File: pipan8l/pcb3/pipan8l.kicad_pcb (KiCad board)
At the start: 2 copper layers, 262.3 x 76.2 mm, 64 parts, among them J1 2x18edgecon, J2 2x18edgecon, J3 2x18edgecon, J4 2x18edgecon, J5 Conn_02x20_Odd_Even, J6 Conn_01x02_Pin, J7 Conn_01x16, J8 Conn_01x12, Q1 2N3906, Q10 2N3906, Q11 2N3906, Q12 2N3906, Q13 2N3906, Q14 2N3906, Q15 2N3906, Q16 2N3906, Q17 2N7000, Q18 2N7000, Q2 2N3906, Q3 2N3906, Q4 2N3906, Q5 2N3906, Q6 2N3906, Q7 2N3906, Q8 2N3906, Q9 2N3906, U1 MCP23017, U2 MCP23017, U3 MCP23017, U4 MCP23017

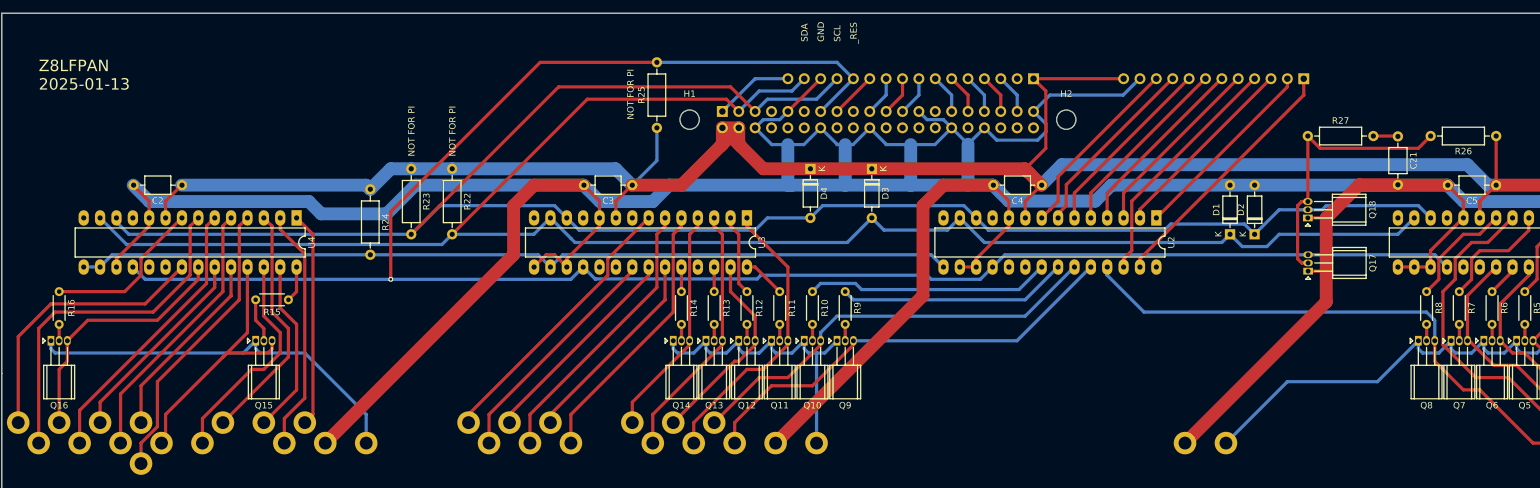
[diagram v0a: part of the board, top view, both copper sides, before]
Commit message: revert pipan8l/pcb3 front-panel piggy-back board to 2025-01-02
it is good enough as is and don't want to make new boards
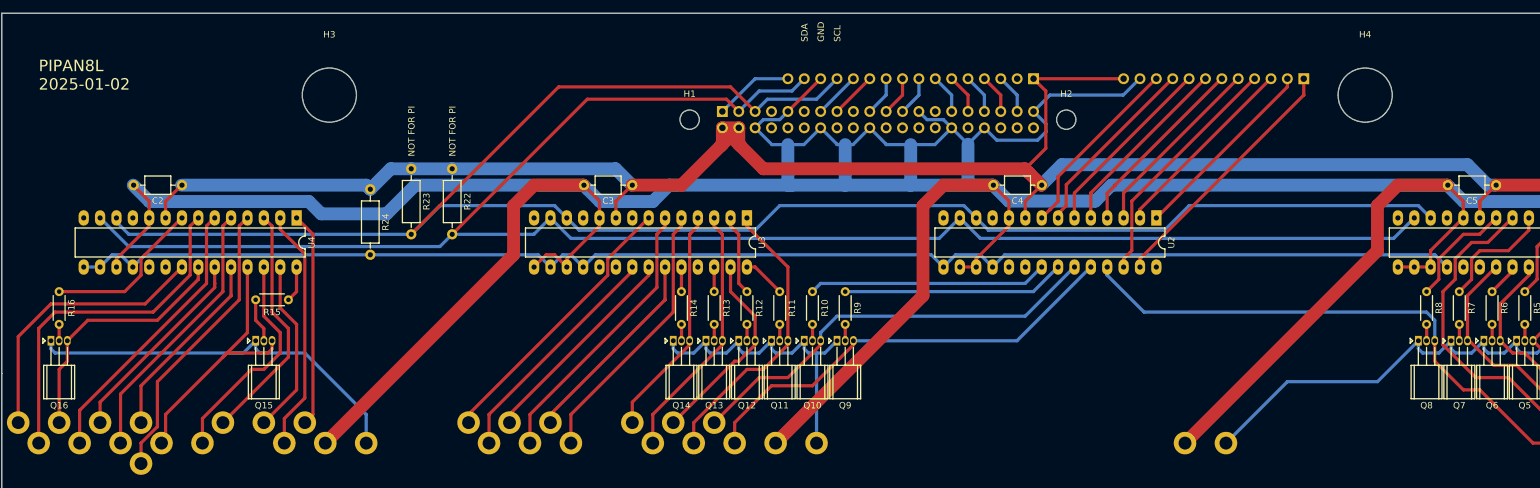
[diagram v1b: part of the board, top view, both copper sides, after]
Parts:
- removed C21: 0.01u, Capacitor_THT:C_Axial_L3.8mm_D2.6mm_P7.50mm_Horizontal
- removed D1, D2, D3, D4: 1N4148, Diode_THT:D_DO-35_SOD27_P7.62mm_Horizontal
- removed Q17, Q18: 2N7000, Package_TO_SOT_THT:TO-92_Inline_W4.0mm_Horizontal_FlatSideDown
- removed R25: 2.2K, Resistor_THT:R_Axial_DIN0207_L6.3mm_D2.5mm_P10.16mm_Horizontal
- removed R26: 100K, Resistor_THT:R_Axial_DIN0207_L6.3mm_D2.5mm_P10.16mm_Horizontal
- removed R27: 100, Resistor_THT:R_Axial_DIN0207_L6.3mm_D2.5mm_P10.16mm_Horizontal
- added H3: MountingHole, MountingHole:MountingHole_8.4mm_M8, F.Cu at (50.8, 12.7)
- added H4: MountingHole, MountingHole:MountingHole_8.4mm_M8, F.Cu at (211.5, 12.7)
- J1: footprint myz8lfpanfoots:backpins-A -> mypipan8lfoots:backpins-A
- J2: footprint myz8lfpanfoots:backpins-B -> mypipan8lfoots:backpins-B
- J3: footprint myz8lfpanfoots:backpins-C -> mypipan8lfoots:backpins-C
- J4: footprint myz8lfpanfoots:backpins-D -> mypipan8lfoots:backpins-D
- R22: value 1.2K -> 1K
- R23: value 680 -> 1K
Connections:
- J5 pad 13: /_RESET -> /GPIO27
- J7 pad 12: /_RESET -> /GPIO27
- U1 pad 18: /_RESET -> /PULLUP
- U2 pad 18: /_RESET -> /PULLUP
- U3 pad 18: /_RESET -> /PULLUP
- U4 pad 18: /_RESET -> /PULLUP
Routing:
- net /_RESET: track 375.2 -> 0.00 mm, vias 1 -> 0
- net /PULLUP: track 136.5 -> 220.8 mm
- net Net-(Q17-G): track 42.8 -> 0.00 mm
- net VCC: track 326.5 -> 308.5 mm
- net GND: track 681.7 -> 672.2 mm
- net /GPIO27: track 0.00 -> 7.18 mm
- net /SDA: track 282.9 -> 279.0 mm
- net Net-(C21-Pad1): track 3.75 -> 0.00 mm
- net /SCL: track 294.1 -> 292.8 mm
- net /RSR09: track 35.6 -> 34.6 mm
- net /RSR10: track 37.9 -> 37.1 mm
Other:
- board text added: "PIPAN8L 2025-01-02"
- board text removed: "Z8LFPAN 2025-01-13"
- board text removed: "_RES"

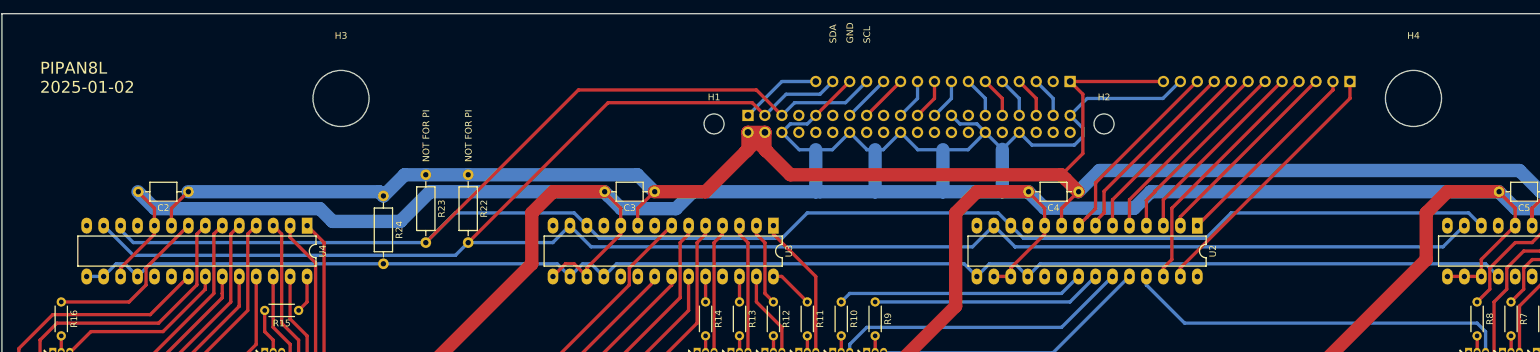
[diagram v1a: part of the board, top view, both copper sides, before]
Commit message: add clipping diodes to i2c bus for zynq-connected front panel
also add _RESET line as 4th pin on connector
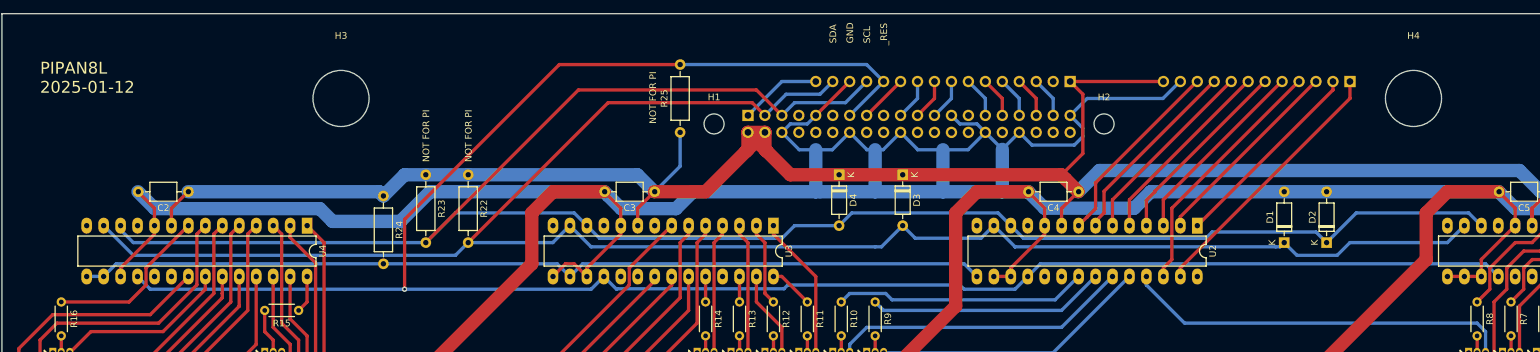
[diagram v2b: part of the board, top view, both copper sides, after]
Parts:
- added D1: 1N4148, Diode_THT:D_DO-35_SOD27_P7.62mm_Horizontal, F.Cu at (192.1, 34.3)
- added D2: 1N4148, Diode_THT:D_DO-35_SOD27_P7.62mm_Horizontal, F.Cu at (198.4, 34.3)
- added D3: 1N4148, Diode_THT:D_DO-35_SOD27_P7.62mm_Horizontal, F.Cu at (134.9, 24.1)
- added D4: 1N4148, Diode_THT:D_DO-35_SOD27_P7.62mm_Horizontal, F.Cu at (125.4, 24.1)
- added R25: 2.2K, Resistor_THT:R_Axial_DIN0207_L6.3mm_D2.5mm_P10.16mm_Horizontal, F.Cu at (101.6, 17.8)
- R22: value 1K -> 1.2K
- R23: value 1K -> 680
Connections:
- U1 pad 18: /PULLUP -> /GPIO27
- U2 pad 18: /PULLUP -> /GPIO27
- U3 pad 18: /PULLUP -> /GPIO27
- U4 pad 18: /PULLUP -> /GPIO27
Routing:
- net /GPIO27: track 7.18 -> 375.2 mm, vias 0 -> 1
- net /PULLUP: track 220.8 -> 137.7 mm
- net VCC: track 308.5 -> 319.0 mm
- net /SDA: track 279.0 -> 282.2 mm
- net /SCL: track 292.8 -> 294.1 mm
- net /RSR09: track 34.6 -> 35.6 mm
- net /RSR10: track 37.1 -> 37.9 mm
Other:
- board text added: "PIPAN8L 2025-01-12"
- board text added: "_RES"
- board text removed: "PIPAN8L 2025-01-02"

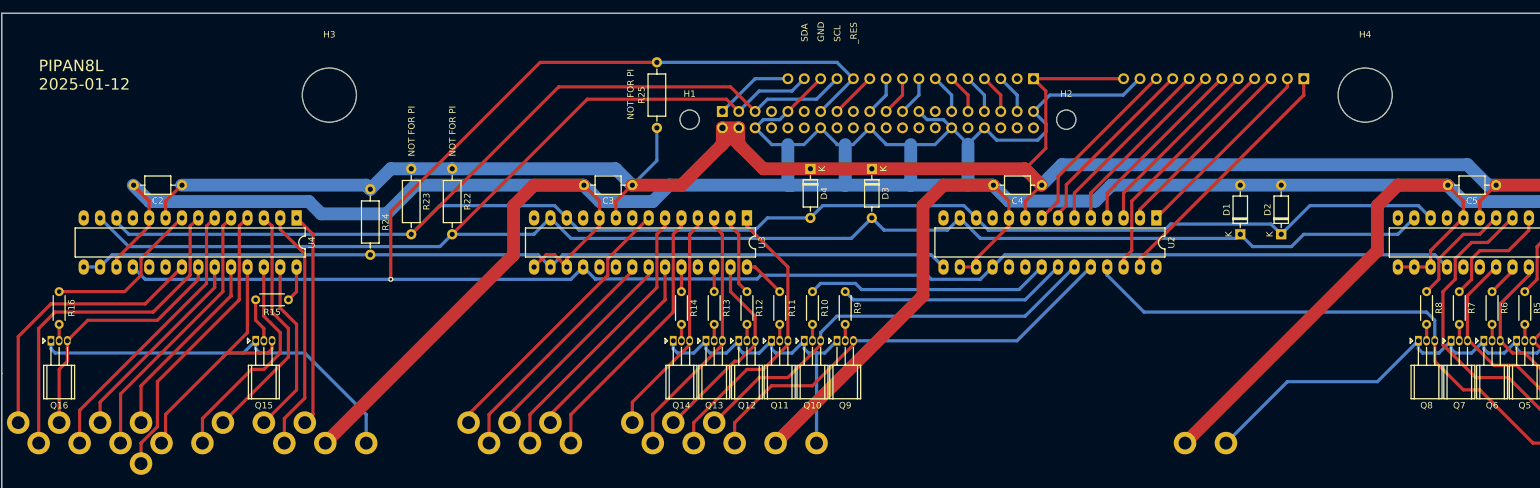
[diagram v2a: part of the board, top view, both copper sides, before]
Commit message: update pipan8l pcb3 reset circuit
hold clock low for 1mS to trigger reset
do not need 4th wire though pins are still there
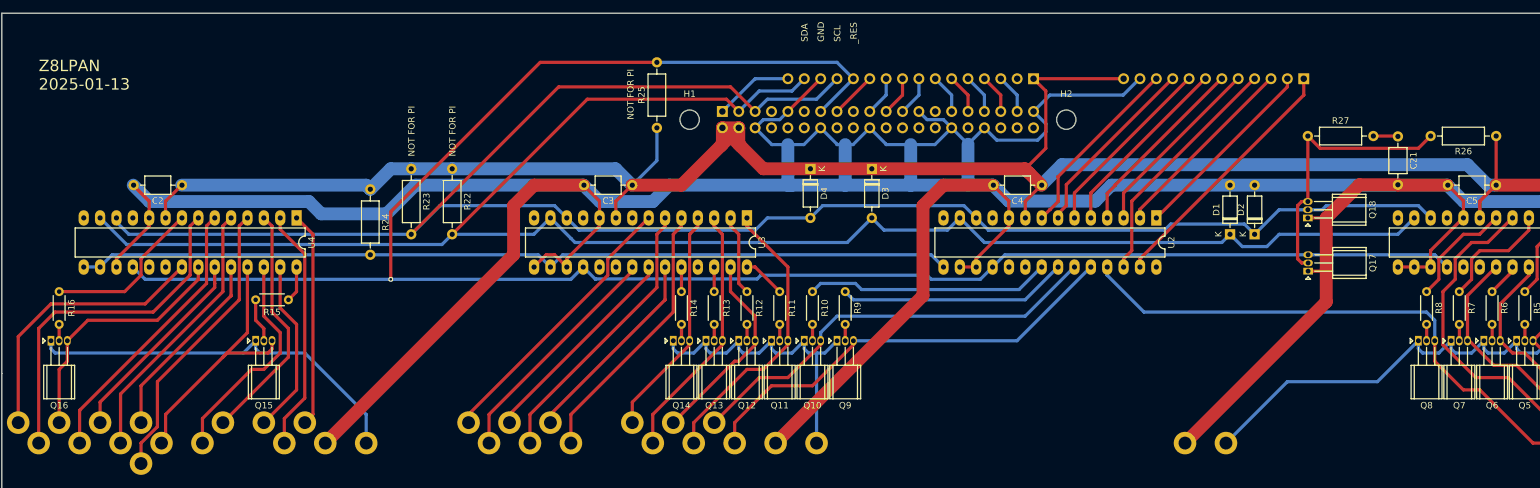
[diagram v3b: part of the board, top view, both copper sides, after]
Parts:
- removed H3, H4: MountingHole, MountingHole:MountingHole_8.4mm_M8
- added C21: 0.01u, Capacitor_THT:C_Axial_L3.8mm_D2.6mm_P7.50mm_Horizontal, F.Cu at (216.5, 19.1)
- added Q17: 2N7000, Package_TO_SOT_THT:TO-92_Inline_W4.0mm_Horizontal_FlatSideDown, F.Cu at (202.6, 40.0)
- added Q18: 2N7000, Package_TO_SOT_THT:TO-92_Inline_W4.0mm_Horizontal_FlatSideDown, F.Cu at (202.6, 31.8)
- added R26: 100K, Resistor_THT:R_Axial_DIN0207_L6.3mm_D2.5mm_P10.16mm_Horizontal, F.Cu at (231.8, 19.1)
- added R27: 100, Resistor_THT:R_Axial_DIN0207_L6.3mm_D2.5mm_P10.16mm_Horizontal, F.Cu at (202.6, 19.1)
- moved D2 4.13 mm to (194.3, 34.3)
- moved D1 1.59 mm to (190.5, 34.3)
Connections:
- net /GPIO27 renamed /_RESET
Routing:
- net Net-(Q17-G): track 0.00 -> 42.8 mm
- net GND: track 672.2 -> 681.7 mm
- net VCC: track 319.0 -> 326.5 mm
- net Net-(C21-Pad1): track 0.00 -> 3.75 mm
- net /PULLUP: track 137.7 -> 136.5 mm
- net /SDA: track 282.2 -> 282.9 mm
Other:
- board text added: "Z8LPAN 2025-01-13"
- board text removed: "PIPAN8L 2025-01-12"
